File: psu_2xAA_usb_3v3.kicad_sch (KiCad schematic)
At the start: 14 parts, among them Q1 CJ2302, Q2 CJ2305, SW1 POWER, U1 HX9193-33GB, U2 QX2304

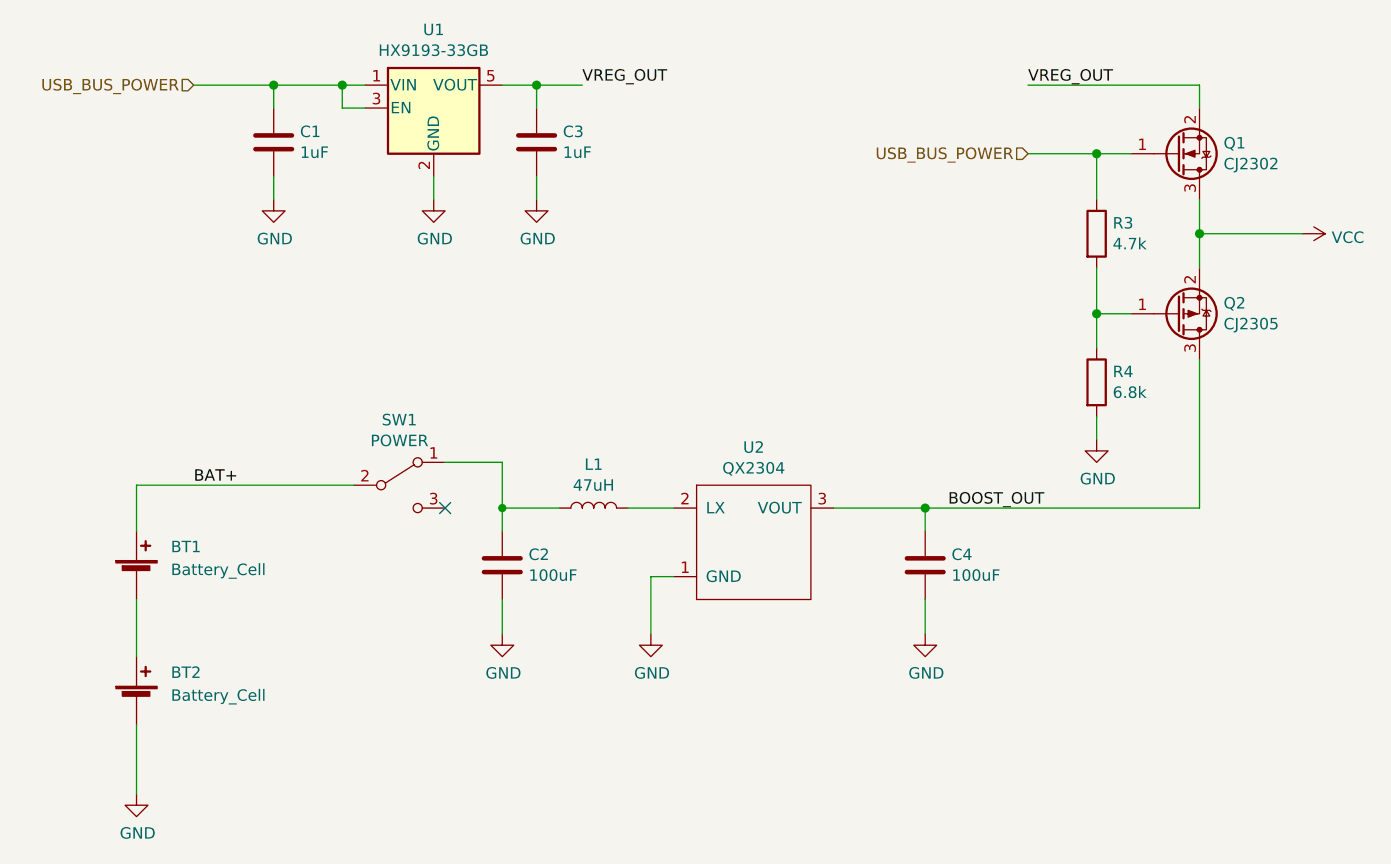
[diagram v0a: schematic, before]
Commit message: Added front artwork and token on the back
Also:
- Tweaked the trace to the antenna to hopefully better match 50ohm impedance
- Tweaked all traces to use fillet on all corners
- Added/fixed parts information

Signed-off-by: Thomas Flummer <tf@flummer.net>
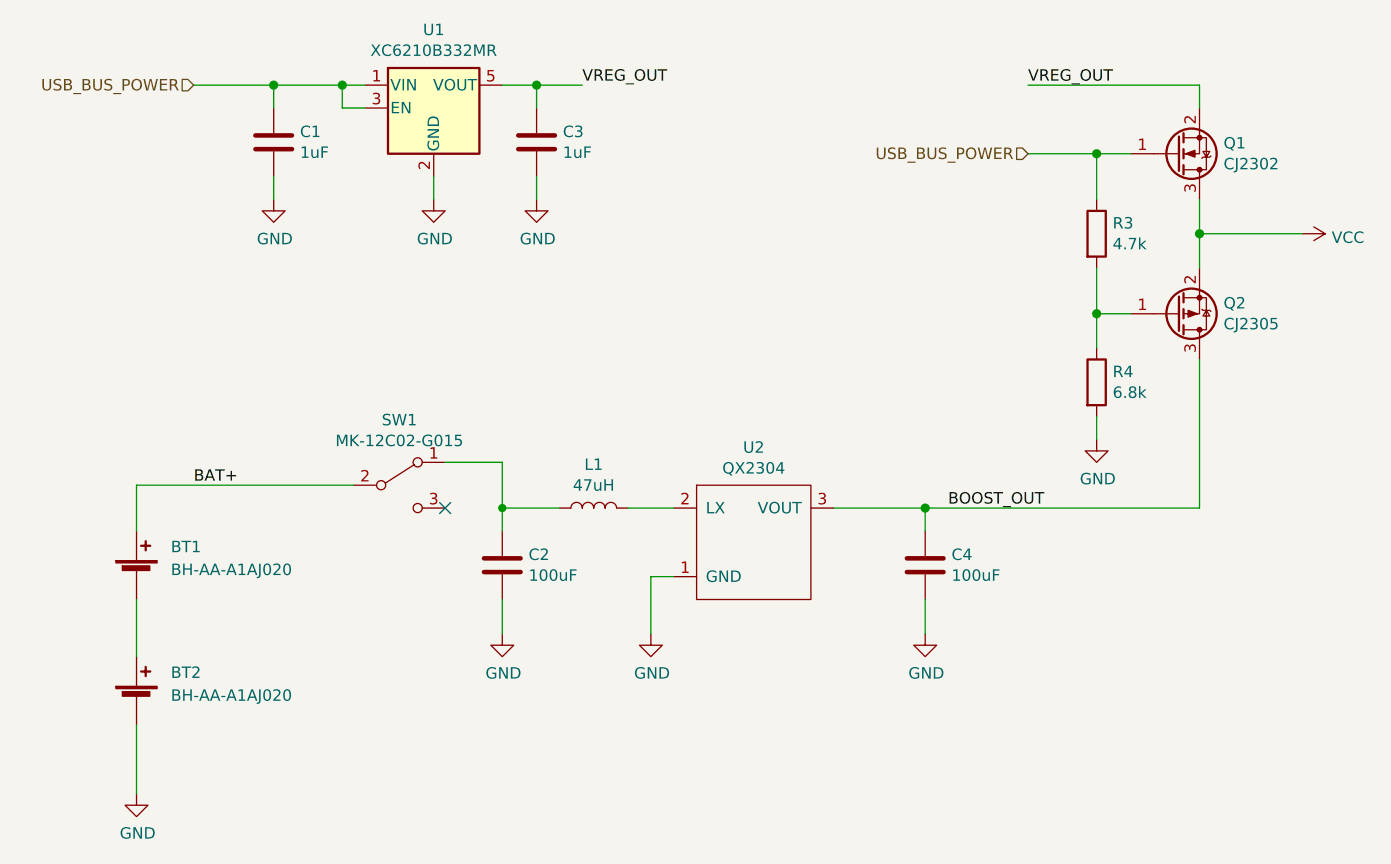
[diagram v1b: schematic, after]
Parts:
- BT1, BT2: value Battery_Cell -> BH-AA-A1AJ020; LCSC (none) -> C5290181
- Q1: LCSC (none) -> C8548
- Q2: LCSC (none) -> C8549
- SW1: value POWER -> MK-12C02-G015; LCSC (none) -> C2911519
- U1: value HX9193-33GB -> XC6210B332MR; LCSC (none) -> C3021084
- U2: LCSC (none) -> C219038
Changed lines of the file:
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@@
+			)
+		)
+		(property "LCSC" "C8549"
+			(at 168.91 76.2 0)
+			(effects
+				(font
+					(size 1.27 1.27)
+				)
+				(hide yes)
 			)
 		)
@@
 			)
 		)
+		(property "LCSC" "C8548"
+			(at 168.91 58.42 0)
+			(effects
+				(font
+					(size 1.27 1.27)
+				)
+				(hide yes)
+			)
+		)
 		(pin "1"
 		)
@@
 			)
 		)
-		(property "Value" "POWER"
+		(property "Value" "MK-12C02-G015"
 			(at 82.55 90.3224 0)
 			(effects
@@
 			)
 		)
-		(property "Datasheet" "~"
+		(property "Datasheet" "https://www.lcsc.com/datasheet/lcsc_datasheet_2111021330_G-Switch-MK-12C02-G015_C2911519.pdf"
 			(at 82.55 95.25 0)
 			(effects
@@
 					(size 1.27 1.27)
 				)
+			)
+		)
+		(property "LCSC" "C2911519"
+			(at 82.55 95.25 0)
+			(effects
+				(font
+					(size 1.27 1.27)
+				)
+				(hide yes)
 			)
 		)
@@
 			)
 		)
-		(property "Value" "Battery_Cell"
+		(property "Value" "BH-AA-A1AJ020"
 			(at 57.15 104.6479 0)
 			(effects
@@
 			)
 		)
-		(property "Datasheet" "~"
+		(property "Datasheet" "https://www.lcsc.com/datasheet/lcsc_datasheet_2411271911_MYOUNG-BH-AA-A1AJ020_C5290181.pdf"
 			(at 53.34 103.886 90)
 			(effects
@@
 					(size 1.27 1.27)
 				)
+			)
+		)
+		(property "LCSC" "C5290181"
+			(at 53.34 105.41 0)
+			(effects
+				(font
+					(size 1.27 1.27)
+				)
+				(hide yes)
 			)
 		)
@@
 			)
 		)
-		(property "Value" "Battery_Cell"
+		(property "Value" "BH-AA-A1AJ020"
 			(at 57.15 118.6179 0)
 			(effects
@@
 			)
 		)
-		(property "Datasheet" "~"
+		(property "Datasheet" "https://www.lcsc.com/datasheet/lcsc_datasheet_2411271911_MYOUNG-BH-AA-A1AJ020_C5290181.pdf"
 			(at 53.34 117.856 90)
 			(effects
@@
 					(size 1.27 1.27)
 				)
+			)
+		)
+		(property "LCSC" "C5290181"
+			(at 53.34 119.38 0)
+			(effects
+				(font
+					(size 1.27 1.27)
+				)
+				(hide yes)
 			)
 		)
@@
 			)
 		)
+		(property "LCSC" "C219038"
+			(at 121.92 101.6 0)
+			(effects
+				(font
+					(size 1.27 1.27)
+				)
+				(hide yes)
+			)
+		)
 		(pin "1"
 		)
@@
 			)
 		)
-		(property "Value" "HX9193-33GB"
+		(property "Value" "XC6210B332MR"
 			(at 86.36 46.9646 0)
 			(effects
@@
 			)
 		)
-		(property "Datasheet" "https://datasheet.lcsc.com/szlcsc/1811131153_HX-hengjiaxing-HX9193-33GB_C296123.pdf"
+		(property "Datasheet" "https://www.lcsc.com/datasheet/lcsc_datasheet_2409302230_TECH-PUBLIC-XC6210B332MR_C3021084.pdf"
 			(at 86.36 50.8 0)
 			(effects
@@
 			)
 		)
+		(property "LCSC" "C3021084"
+			(at 86.36 53.34 0)
+			(effects
+				(font
+					(size 1.27 1.27)
+				)
+				(hide yes)
+			)
+		)
